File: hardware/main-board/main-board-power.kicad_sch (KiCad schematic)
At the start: 31 parts, among them J3 Power Board, J4 DMX512, U4 TPS54294

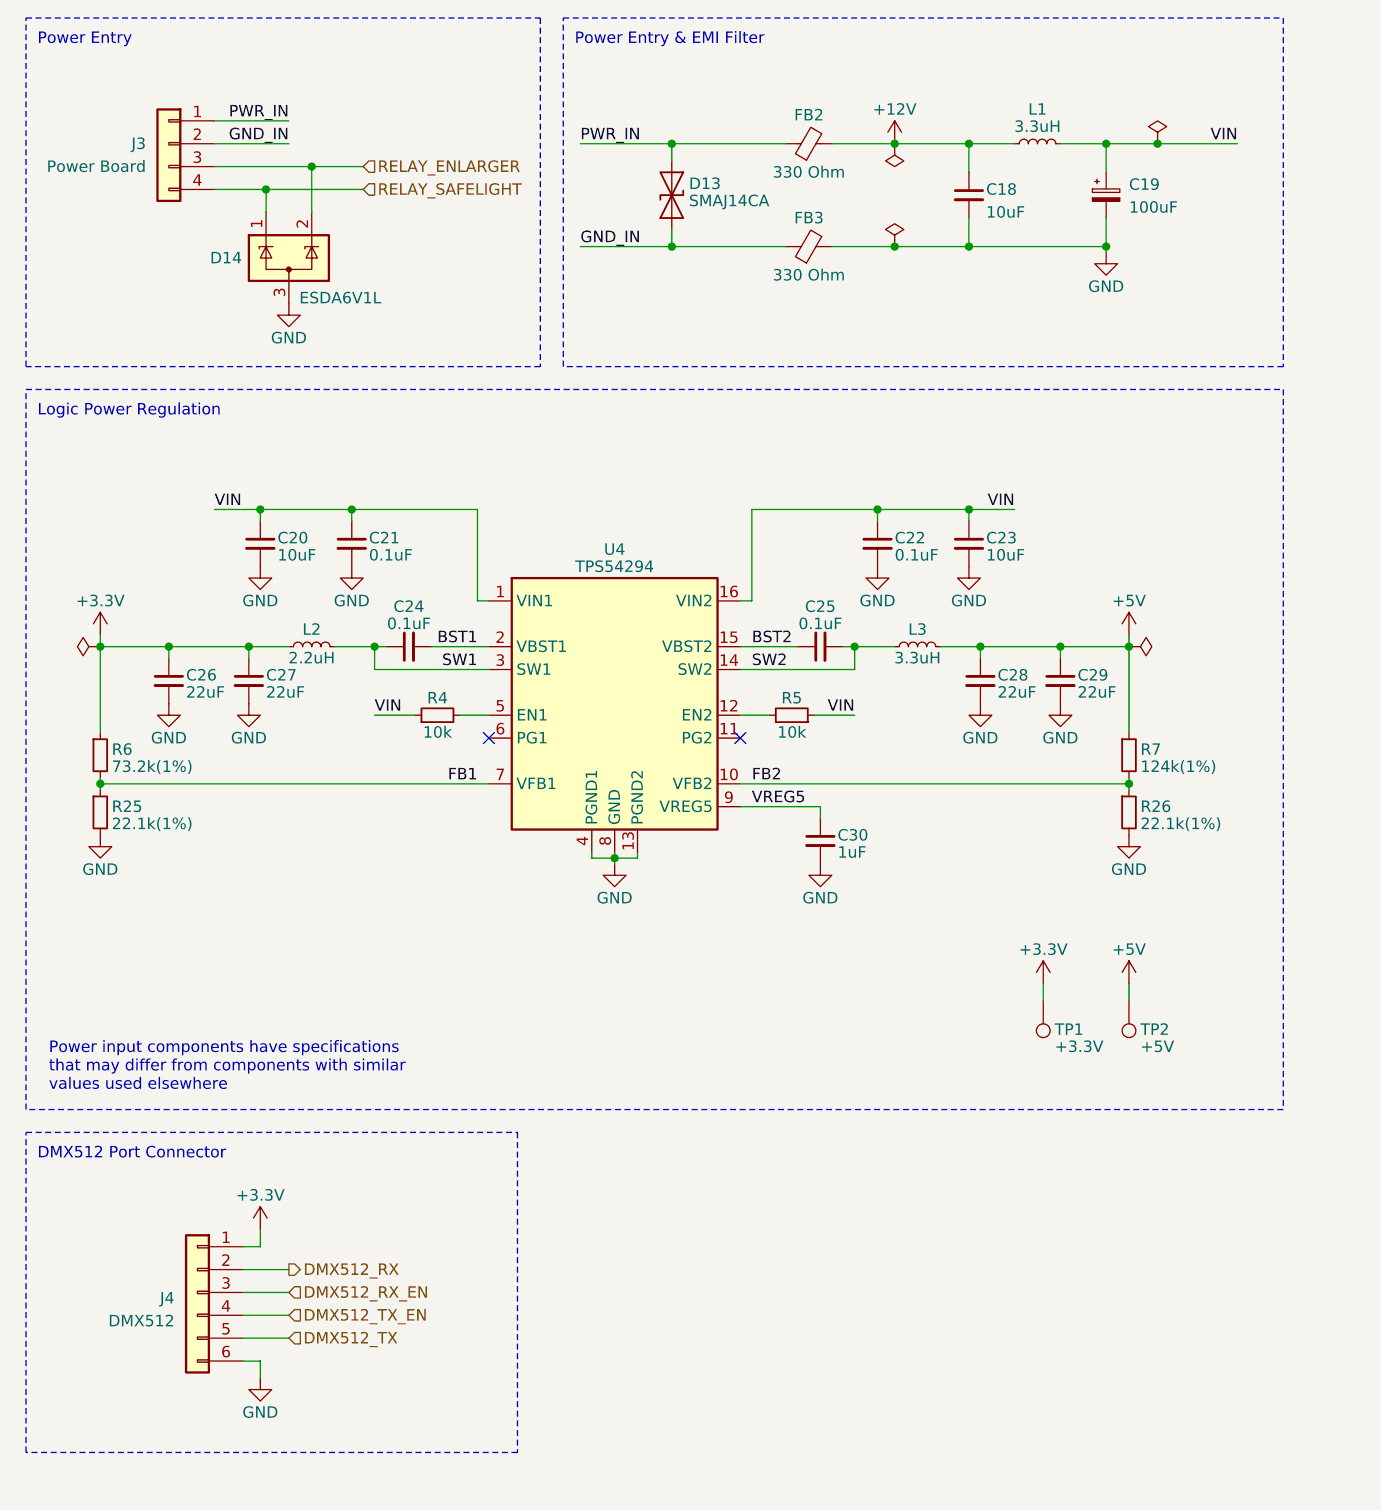
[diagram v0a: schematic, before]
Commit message: Apply suggested changes to buck converter circuit
This applies the following changes:
- Sequence 3.3V and 5V rails
- Implement cold startup delay
- Add feedforward capacitors

Refs #72
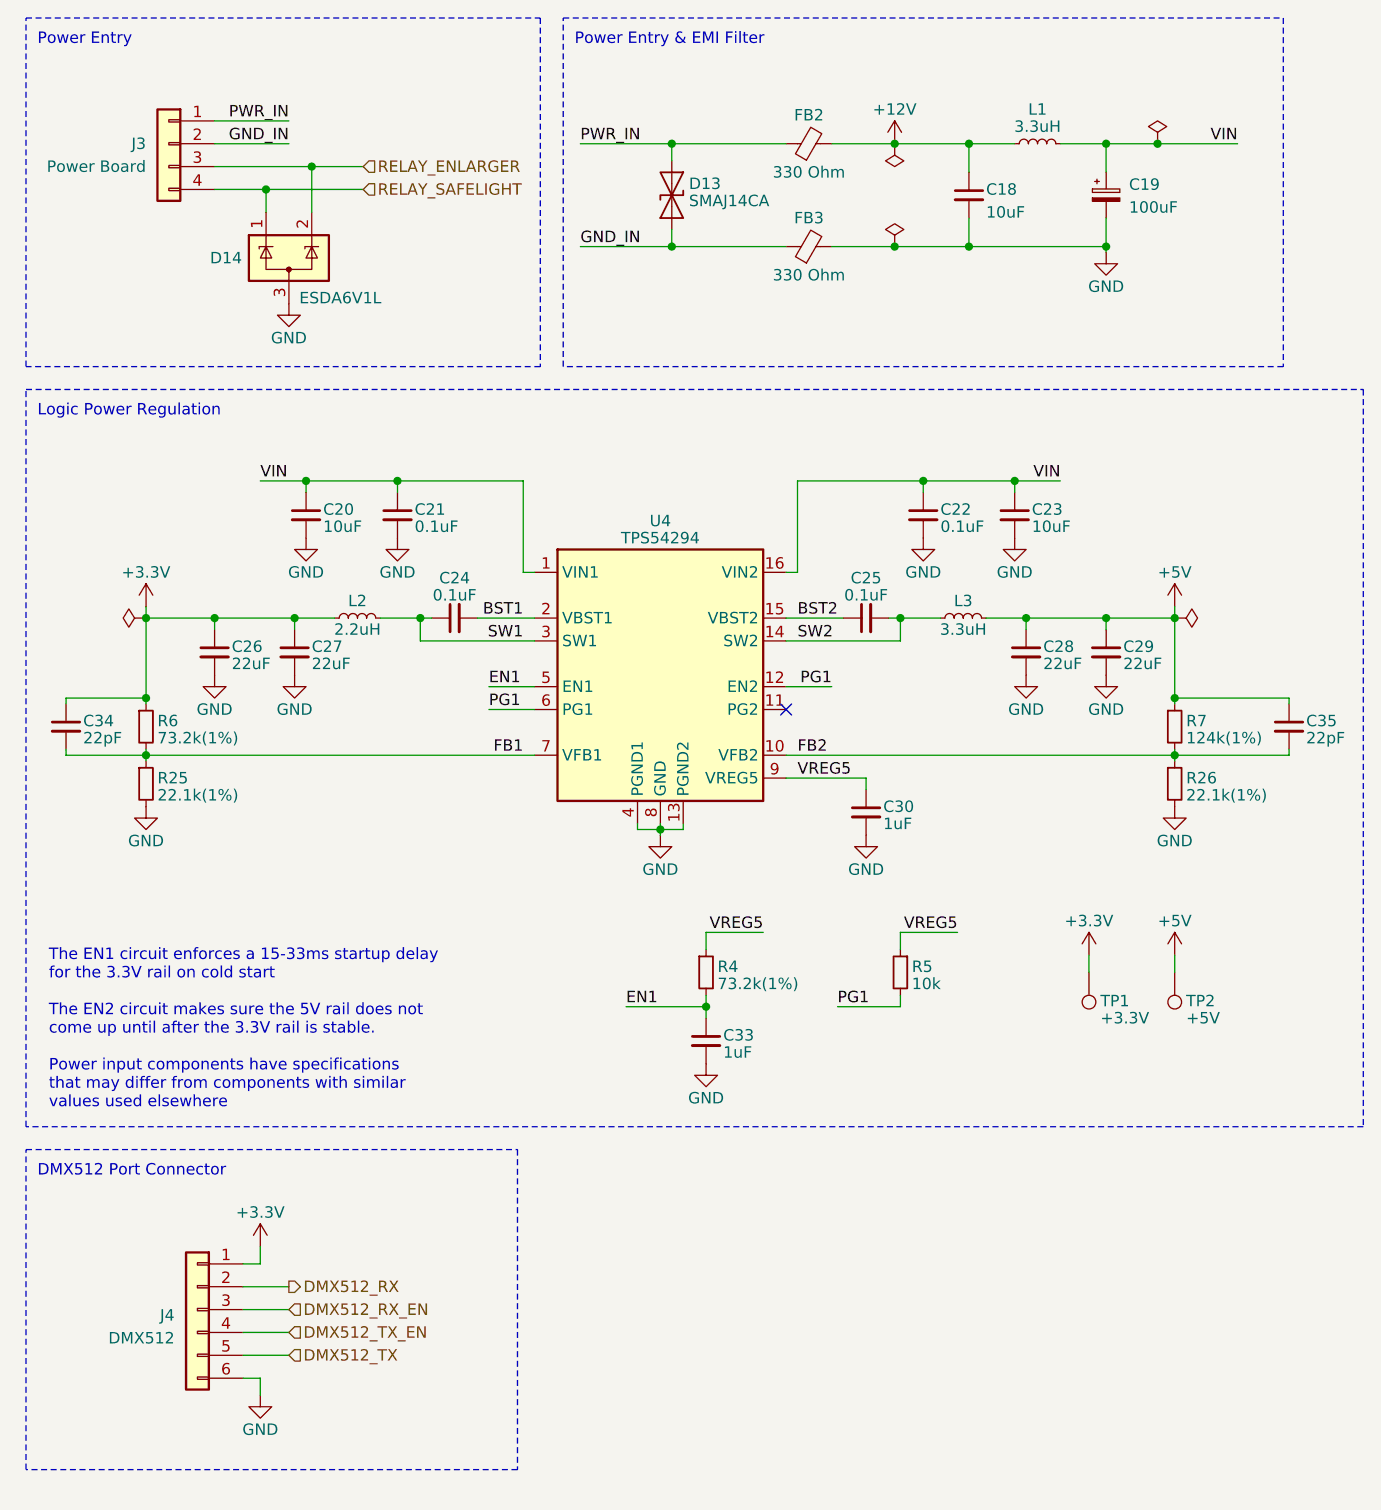
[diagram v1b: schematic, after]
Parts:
- added C33: 1uF, Capacitor_SMD:C_0603_1608Metric, symbol Device:C_Small
- added C34, C35: 22pF, Capacitor_SMD:C_0603_1608Metric, symbol Device:C_Small
- R4: value 10k -> 73.2k(1%); Manufacturer Vishay Dale -> YAGEO; Manufacturer PN CRCW060310K0JNEA -> RC0603FR-0773K2L; Supplier PN 541-10KGCT-ND -> 311-73.2KHRCT-ND
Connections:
- net +3.3V: now also C34.1
- net +5V: now also C35.1
- net FB1: now also C34.2
- net FB2: now also C35.2
- net GND: now also C33.2
- net VIN: no longer R4.1, R5.1
- net VREG5: now also R4.1, R5.1
- net PG1: now reaches R5.2, U4.12 (EN2)
- net PG1: now also U4.6 (PG1)
- net EN1: now reaches R4.2, U4.5 (EN1)
- net EN1: now also C33.1
- no-connect marks 2 -> 1
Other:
- note added: "The EN1 circuit enforces a 15-33ms startup delay for the 3.3V rail on cold start The EN2 circuit makes sure the 5V rail does not come up until after the 3.3V rail is stable. Power input components have specifications that may differ from components with similar values used elsewhere"
- note removed: "Power input components have specifications that may differ from components with similar values used elsewhere"
- moved on the sheet: C20, C21, C22, C23, C24, C25, C26, C27, C28, C29, C30, J4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

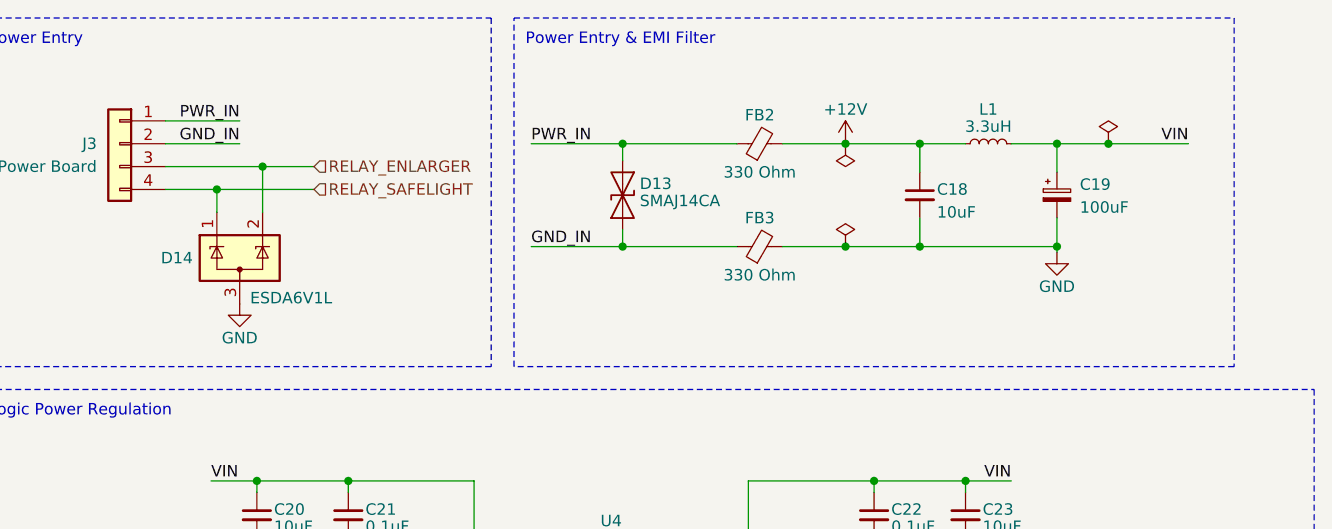
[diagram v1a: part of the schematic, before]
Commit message: Cleaned up main board power input
Removed ferrite beads
Replaced TVS diode with a unidirectional one with a lower voltage
Cleaned up routing to use more fill areas on the input path

Ref #74
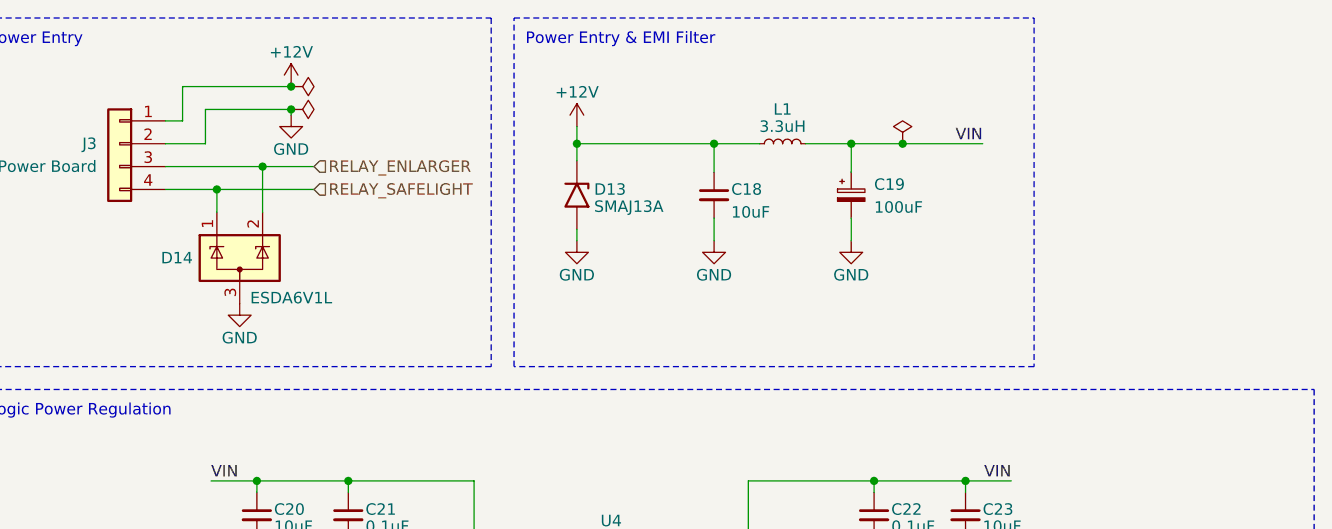
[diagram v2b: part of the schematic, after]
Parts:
- removed D13: SMAJ14CA, Diode_SMD:D_SMA, symbol Diode:SMAJ14CA
- removed FB2, FB3: 330 Ohm, Inductor_SMD:L_0603_1608Metric, symbol Device:FerriteBead_Small
- added D13: SMAJ13A, Diode_SMD:D_SMA, symbol Diode:SMAJ13A
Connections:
- net GND_IN is gone; now on net GND: J3.2 (Pin_2)
- net PWR_IN is gone; now on net +12V: J3.1 (Pin_1)
- net +12V: now also D13.1 (A1)
- net GND: now also D13.2 (A2)
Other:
- moved on the sheet: C18, C19, L1

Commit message: Misc schematic cleanup
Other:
- note added: "Power Entry Connector"
- note added: "This connector goes to the power board, which is where the RS-485 transceiver and the XLR jack are located."
- note removed: "Power Entry"
- moved on the sheet: J4
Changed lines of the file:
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@@
 	(title_block
 		(title "Printalyzer - Main Board (Power Supply and Control)")
-		(date "2024-04-16")
-		(rev "D")
+		(date "2024-09-01")
+		(rev "F")
 		(company "Dektronics, Inc.")
 		(comment 1 "Derek Konigsberg")
@@
 	(wire
 		(pts
-			(xy 40.005 161.925) (xy 45.085 161.925)
+			(xy 32.385 160.02) (xy 37.465 160.02)
 		)
 		(stroke
@@
 	(wire
 		(pts
-			(xy 41.91 154.305) (xy 41.91 152.4)
+			(xy 34.29 152.4) (xy 34.29 150.495)
 		)
 		(stroke
@@
 	(wire
 		(pts
-			(xy 40.005 164.465) (xy 45.085 164.465)
+			(xy 32.385 162.56) (xy 37.465 162.56)
 		)
 		(stroke
@@
 	(wire
 		(pts
-			(xy 40.005 159.385) (xy 45.085 159.385)
+			(xy 32.385 157.48) (xy 37.465 157.48)
 		)
 		(stroke
@@
 	(wire
 		(pts
-			(xy 41.91 167.005) (xy 41.91 168.91)
+			(xy 34.29 165.1) (xy 34.29 167.005)
 		)
 		(stroke
@@
 	(wire
 		(pts
-			(xy 40.005 156.845) (xy 45.085 156.845)
+			(xy 32.385 154.94) (xy 37.465 154.94)
 		)
 		(stroke
@@
 	(wire
 		(pts
-			(xy 40.005 167.005) (xy 41.91 167.005)
+			(xy 32.385 165.1) (xy 34.29 165.1)
 		)
 		(stroke
@@
 	(wire
 		(pts
-			(xy 40.005 154.305) (xy 41.91 154.305)
+			(xy 32.385 152.4) (xy 34.29 152.4)
 		)
 		(stroke
@@
 	(rectangle
 		(start 15.875 141.605)
-		(end 70.485 177.165)
+		(end 59.055 179.705)
 		(stroke
 			(width 0)
@@
 		)
 	)
+	(text "This connector goes to the power board,\nwhich is where the RS-485 transceiver\nand the XLR jack are located."
+		(exclude_from_sim no)
+		(at 17.145 175.895 0)
+		(effects
+			(font
+				(size 1.27 1.27)
+			)
+			(justify left)
+		)
+	)
 	(text "The EN1 circuit enforces a 15-33ms startup delay\nfor the 3.3V rail on cold start\n\nThe EN2 circuit makes sure the 5V rail does not\ncome up until after the 3.3V rail is stable.\n\nPower input components have specifications\nthat may differ from components with similar\nvalues used elsewhere"
 		(exclude_from_sim no)
@@
 		)
 	)
-	(text "Power Entry"
+	(text "Power Entry Connector"
 		(exclude_from_sim no)
 		(at 17.145 19.05 0)
@@
 	(hierarchical_label "DMX512_RX"
 		(shape output)
-		(at 45.085 156.845 0)
+		(at 37.465 154.94 0)
 		(fields_autoplaced yes)
 		(effects
@@
 	(hierarchical_label "DMX512_TX"
 		(shape input)
-		(at 45.085 164.465 0)
+		(at 37.465 162.56 0)
 		(fields_autoplaced yes)
 		(effects
@@
 	(hierarchical_label "DMX512_TX_EN"
 		(shape input)
-		(at 45.085 161.925 0)
+		(at 37.465 160.02 0)
 		(fields_autoplaced yes)
 		(effects
@@
 	(hierarchical_label "DMX512_RX_EN"
 		(shape input)
-		(at 45.085 159.385 0)
+		(at 37.465 157.48 0)
 		(fields_autoplaced yes)
 		(effects
@@
 	(symbol
 		(lib_id "power:GND")
-		(at 41.91 168.91 0)
+		(at 34.29 167.005 0)
 		(unit 1)
 		(exclude_from_sim no)
@@
 		(dnp no)
 		(property "Reference" "#PWR052"
-			(at 41.91 175.26 0)
+			(at 34.29 173.355 0)
 			(effects
 				(font
@@
 		)
 		(property "Value" "GND"
-			(at 41.91 172.72 0)
+			(at 34.29 170.815 0)
 			(effects
 				(font
@@
 		)
 		(property "Footprint" ""
-			(at 41.91 168.91 0)
+			(at 34.29 167.005 0)
 			(effects
 				(font
@@
 		)
 		(property "Datasheet" ""
-			(at 41.91 168.91 0)
+			(at 34.29 167.005 0)
 			(effects
 				(font
@@
 		)
 		(property "Description" "Power symbol creates a global label with name \"GND\" , ground"
-			(at 41.91 168.91 0)
+			(at 34.29 167.005 0)
 			(effects
 				(font
@@
 	(symbol
 		(lib_id "power:+3.3V")
-		(at 41.91 152.4 0)
+		(at 34.29 150.495 0)
 		(unit 1)
 		(exclude_from_sim no)
@@
 		(dnp no)
 		(property "Reference" "#PWR051"
-			(at 41.91 156.21 0)
+			(at 34.29 154.305 0)
 			(effects
 				(font
@@
 		)
 		(property "Value" "+3.3V"
-			(at 41.91 148.59 0)
+			(at 34.29 146.685 0)
 			(effects
 				(font
@@
 		)
 		(property "Footprint" ""
-			(at 41.91 152.4 0)
+			(at 34.29 150.495 0)
 			(effects
 				(font
@@
 		)
 		(property "Datasheet" ""
-			(at 41.91 152.4 0)
+			(at 34.29 150.495 0)
 			(effects
 				(font
@@
 		)
 		(property "Description" "Power symbol creates a global label with name \"+3.3V\""
-			(at 41.91 152.4 0)
+			(at 34.29 150.495 0)
 			(effects
 				(font
@@
 	(symbol
 		(lib_id "Connector_Generic:Conn_01x06")
-		(at 34.925 159.385 0)
+		(at 27.305 157.48 0)
 		(mirror y)
 		(unit 1)
@@
 		(dnp no)
 		(property "Reference" "J4"
-			(at 32.385 160.02 0)
+			(at 24.765 158.115 0)
 			(effects
 				(font
@@
 		)
 		(property "Value" "DMX512"
-			(at 32.385 162.56 0)
+			(at 24.765 160.655 0)
 			(effects
 				(font
@@
 		)
 		(property "Footprint" "Connector_JST:JST_SH_BM06B-SRSS-TB_1x06-1MP_P1.00mm_Vertical"
-			(at 34.925 159.385 0)
+			(at 27.305 157.48 0)
 			(effects
 				(font
@@
 		)
 		(property "Datasheet" "https://www.jst-mfg.com/product/pdf/eng/eSH.pdf"
-			(at 34.925 159.385 0)
+			(at 27.305 157.48 0)
 			(effects
 				(font
@@
 		)
 		(property "Description" "CONN HEADER SMD 6POS 1MM"
-			(at 34.925 159.385 0)
+			(at 27.305 157.48 0)
 			(effects
 				(font
@@
 		)
 		(property "Manufacturer" "JST Sales America Inc."
-			(at 34.925 159.385 0)
+			(at 27.305 157.48 0)
 			(effects
 				(font
@@
 		)
 		(property "Manufacturer PN" "BM06B-SRSS-TB(LF)(SN)"
-			(at 34.925 159.385 0)
+			(at 27.305 157.48 0)
 			(effects
 				(font
@@
 		)
 		(property "Supplier" "Digi-Key"
-			(at 34.925 159.385 0)
+			(at 27.305 157.48 0)
 			(effects
 				(font
@@
 		)
 		(property "Supplier PN" "455-1792-1-ND"
-			(at 34.925 159.385 0)
+			(at 27.305 157.48 0)
 			(effects
 				(font

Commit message: BOM fixup
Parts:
- R5: value 10k -> 10K
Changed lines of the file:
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@@
 			)
 		)
-		(property "Value" "10k"
+		(property "Value" "10K"
 			(at 114.3 123.19 0)
 			(effects
@@
 			)
 		)
-		(property "Description" "RES SMD 10K OHM 5% 1/16W 0603"
+		(property "Description" "RES SMD 10K OHM 5% 1/10W 0603"
 			(at 113.03 121.92 0)
 			(effects

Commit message: Update schematic and layout dates and generate images
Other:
- title: Printalyzer - Main Board (Power Supply and Control) -> Printalyzer - Main Board
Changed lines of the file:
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@@
 	(paper "USLetter")
 	(title_block
-		(title "Printalyzer - Main Board (Power Supply and Control)")
-		(date "2024-09-01")
+		(title "Printalyzer - Main Board")
+		(date "2024-09-08")
 		(rev "F")
 		(company "Dektronics, Inc.")
